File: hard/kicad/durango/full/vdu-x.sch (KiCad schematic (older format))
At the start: 48 parts, among them J105 SCART, J4 LED, Q306 BC548, Q4 BC548, Q5 BC548, U124 74HC574, U125 74HC157, U126 HC86, U127 74HC245, U15 74HCT4040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

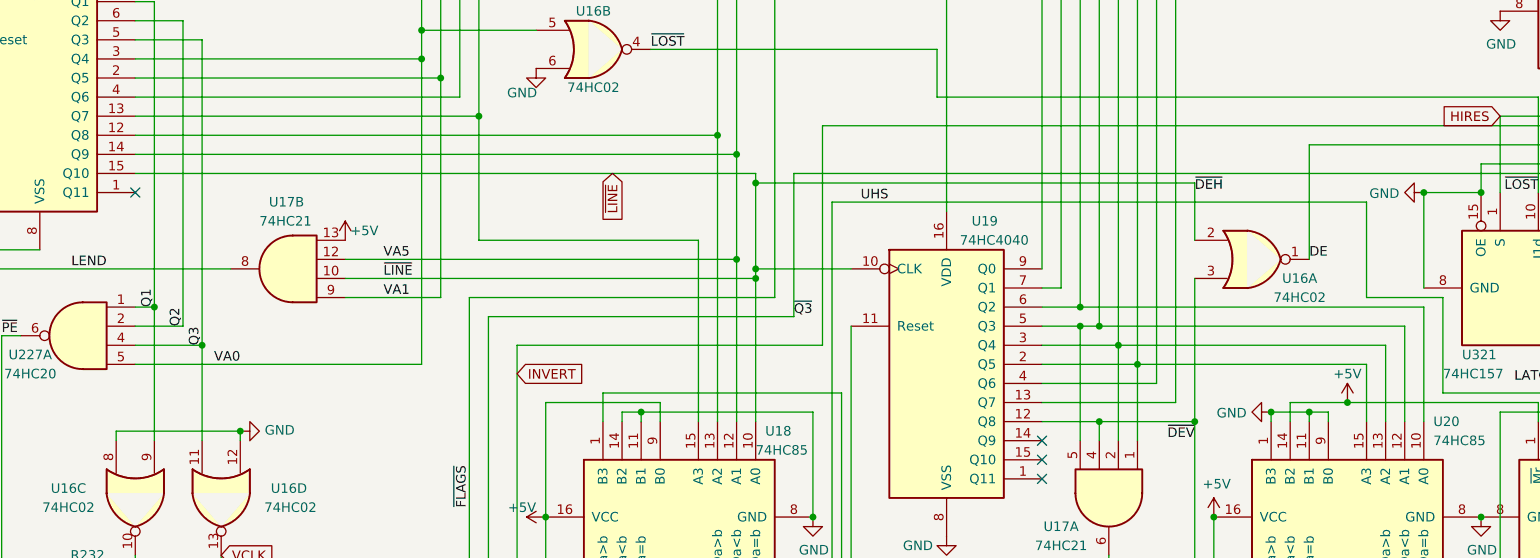
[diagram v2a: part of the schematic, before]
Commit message: PINOUT: rewire HC85s
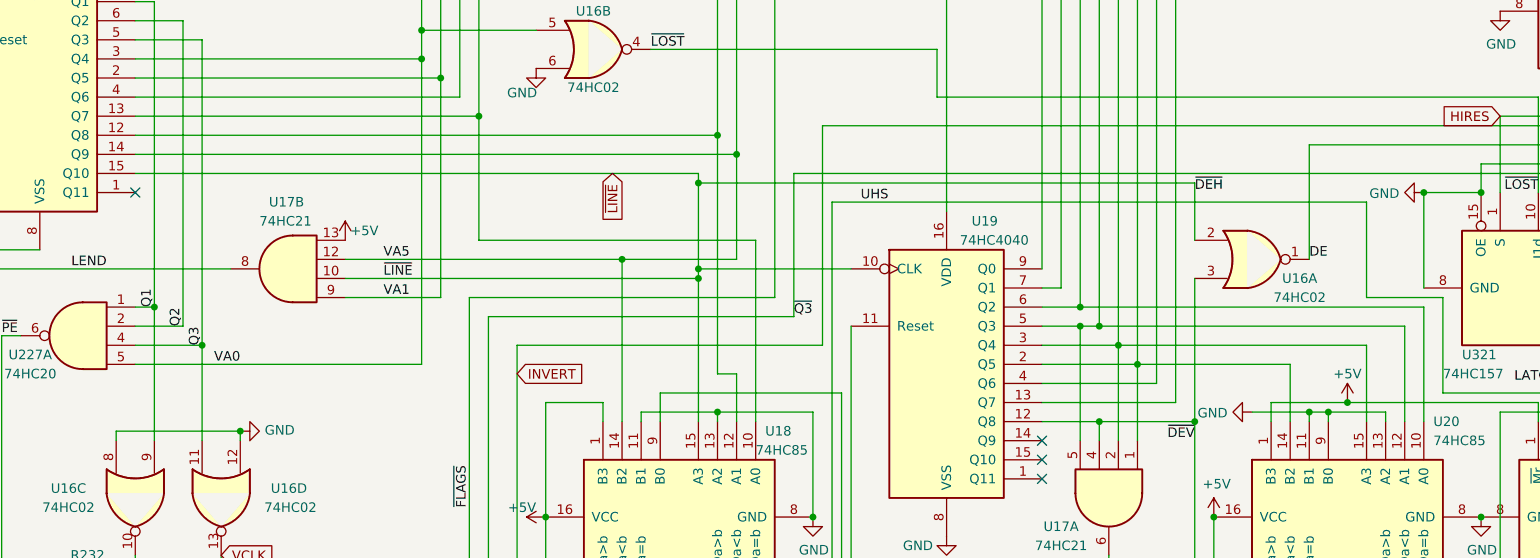
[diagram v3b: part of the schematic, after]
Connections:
- net +5V: now also U18.1 (B3), U20.1 (B3); no longer U18.9 (B0), U20.14 (B2)
- net GND: now also U18.13 (A2), U20.13 (A2); no longer U18.14 (B2), U20.1 (B3)
- net VA10: now also U20.15 (A3); no longer U20.13 (A2)
- net VA11: now also U20.14 (B2); no longer U20.15 (A3)
- net VA3: now also U18.10 (A0); no longer U18.15 (A3)
- net VA4: now also U18.12 (A1); no longer U18.13 (A2)
- net VA5: now also U18.14 (B2); no longer U18.12 (A1)
- net ~LINE: now also U18.15 (A3); no longer U18.10 (A0)
- net ~VS: now also U18.9 (B0); no longer U18.1 (B3)
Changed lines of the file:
@@
 Connection ~ 4650 3900
 Wire Wire Line
-	5250 3400 5250 3300
-Wire Wire Line
 	4650 3300 4650 3900
-Wire Wire Line
-	5150 3400 5150 3350
-Wire Wire Line
-	5150 3350 6050 3350
 Wire Wire Line
 	6050 3350 6050 3900
@@
 	5050 4400 5150 4400
 Wire Wire Line
-	5150 3350 5050 3350
-Wire Wire Line
-	5050 3350 5050 3400
-Connection ~ 5150 3350
-Wire Wire Line
 	8050 3400 8050 4450
 Wire Wire Line
@@
 Connection ~ 8050 3400
 Wire Wire Line
-	7750 3100 8950 3100
-Wire Wire Line
-	8950 3100 8950 3400
-Wire Wire Line
-	7650 3000 9050 3000
-Wire Wire Line
-	9050 3000 9050 3400
+	7750 3100 8550 3100
+Wire Wire Line
+	7650 3000 8950 3000
 Wire Wire Line
 	7550 2900 9150 2900
-Wire Wire Line
-	9150 2900 9150 3400
 Connection ~ 7550 2900
 Wire Wire Line
 	7450 2800 9250 2800
-Wire Wire Line
-	9250 2800 9250 3400
 Connection ~ 7450 2800
-Wire Wire Line
-	8450 3400 8450 3350
-Wire Wire Line
-	8450 3350 8650 3350
-Wire Wire Line
-	8650 3350 8650 3400
-Wire Wire Line
-	8550 3400 8550 3300
 $Comp
 L power:+5V #PWR0122
@@
 L power:GND #PWR0123
 U 1 1 608EF4C1
-P 8450 3350
-F 0 "#PWR0123" H 8450 3100 50  0001 C CNN
-F 1 "GND" V 8455 3222 50  0000 R CNN
-F 2 "" H 8450 3350 50  0001 C CNN
-F 3 "" H 8450 3350 50  0001 C CNN
-	1    8450 3350
+P 8350 3350
+F 0 "#PWR0123" H 8350 3100 50  0001 C CNN
+F 1 "GND" V 8355 3222 50  0000 R CNN
+F 2 "" H 8350 3350 50  0001 C CNN
+F 3 "" H 8350 3350 50  0001 C CNN
+	1    8350 3350
 	0    1    1    0
 $EndComp
-Connection ~ 8450 3350
 Wire Wire Line
 	6250 2900 6250 4250
@@
 	8050 2450 8050 2150
 Wire Wire Line
-	8050 2150 5750 2150
-Connection ~ 5750 2150
-Wire Wire Line
 	10950 3250 10950 5650
 Text GLabel 8800 550  0    50   Input ~ 0
@@
 $EndComp
 Wire Wire Line
-	4300 2450 5450 2450
-Wire Wire Line
-	5450 2450 5450 3400
+	4300 2450 5750 2450
 $Comp
 L 74xx:74LS20 U227
@@
 VA1
 Wire Wire Line
-	3600 2550 5650 2550
-Connection ~ 5650 2550
-Wire Wire Line
-	3600 2650 5750 2650
-Wire Wire Line
-	5750 2150 5750 2600
-Connection ~ 5750 2650
+	3600 2550 5050 2550
+Wire Wire Line
+	3600 2650 5450 2650
 Text Label 3800 2650 0    50   ~ 0
 ~LINE
@@
 Wire Wire Line
 	2500 1900 5550 1900
-Connection ~ 5550 1900
-Wire Wire Line
-	5550 1900 5550 3400
 Wire Wire Line
 	2500 2000 5650 2000
@@
 	5650 2000 5650 2550
 Wire Wire Line
-	2500 2100 5750 2100
-Wire Wire Line
-	5750 2100 5750 2150
+	2500 2100 5450 2100
 NoConn ~ 2500 2200
 Wire Wire Line
@@
 Wire Wire Line
 	4000 1350 4000 1500
-Wire Wire Line
-	5650 2550 5650 3400
 Wire Wire Line
 	6700 1700 6700 1450
@@
 Wire Wire Line
 	1200 2500 2000 2500
-Wire Wire Line
-	5750 2650 5750 3400
 Wire Wire Line
 	4350 2850 5950 2850
@@
 Wire Wire Line
 	7600 4400 6200 4400
-Wire Wire Line
-	6200 4400 6200 3250
 Connection ~ 10050 4400
 Text Label 7050 4400 0    50   ~ 0
 ~VS
 Wire Wire Line
-	4650 3300 5250 3300
-Wire Wire Line
-	4950 3400 4950 3250
-Wire Wire Line
-	4950 3250 6200 3250
+	4650 3300 4950 3300
 Wire Wire Line
 	6150 2250 6150 4400
-Wire Wire Line
-	6250 2600 5750 2600
-Connection ~ 5750 2600
-Wire Wire Line
-	5750 2600 5750 2650
 Text Label 6300 2250 0    50   ~ 0
 UHS
 Wire Wire Line
-	8650 3350 8750 3350
-Wire Wire Line
-	8750 3350 8750 3400
-Connection ~ 8650 3350
-Wire Wire Line
-	8550 3300 8850 3300
+	8450 3300 8850 3300
 Connection ~ 8850 3300
 Wire Wire Line
@@
 Wire Wire Line
 	750  5900 800  5900
+Wire Wire Line
+	5150 3350 5550 3350
+Wire Wire Line
+	4950 3400 4950 3300
+Wire Wire Line
+	5150 3350 5150 3400
+Wire Wire Line
+	5550 3350 5550 3400
+Connection ~ 5550 3350
+Wire Wire Line
+	5550 3350 6050 3350
+Wire Wire Line
+	6200 4400 6200 3250
+Wire Wire Line
+	5250 3250 6200 3250
+Wire Wire Line
+	5250 3400 5250 3250
+Wire Wire Line
+	5050 3400 5050 2550
+Connection ~ 5050 2550
+Wire Wire Line
+	5050 2550 5650 2550
+Connection ~ 5450 2600
+Wire Wire Line
+	6250 2600 5450 2600
+Wire Wire Line
+	5450 2100 5450 2150
+Wire Wire Line
+	5450 2150 5450 2600
+Connection ~ 5450 2150
+Wire Wire Line
+	8050 2150 5450 2150
+Wire Wire Line
+	5450 2600 5450 2650
+Connection ~ 5450 2650
+Wire Wire Line
+	5450 2650 5450 3400
+Wire Wire Line
+	5550 1900 5550 3150
+Wire Wire Line
+	5550 3150 5650 3150
+Wire Wire Line
+	5650 3150 5650 3400
+Connection ~ 5550 1900
+Wire Wire Line
+	5750 2450 5750 3400
+Wire Wire Line
+	8350 3350 8650 3350
+Wire Wire Line
+	8450 3300 8450 3400
+Wire Wire Line
+	8650 3350 8650 3400
+Connection ~ 8650 3350
+Wire Wire Line
+	8650 3350 8750 3350
+Wire Wire Line
+	8750 3350 8750 3400
+Wire Wire Line
+	8750 3350 9050 3350
+Wire Wire Line
+	9050 3350 9050 3400
+Connection ~ 8750 3350
+Wire Wire Line
+	8550 3100 8550 3400
+Wire Wire Line
+	8950 3000 8950 3400
+Wire Wire Line
+	9250 2800 9250 3400
+Wire Wire Line
+	9150 3400 9150 2900
 Wire Bus Line
 	8800 550  10750 550

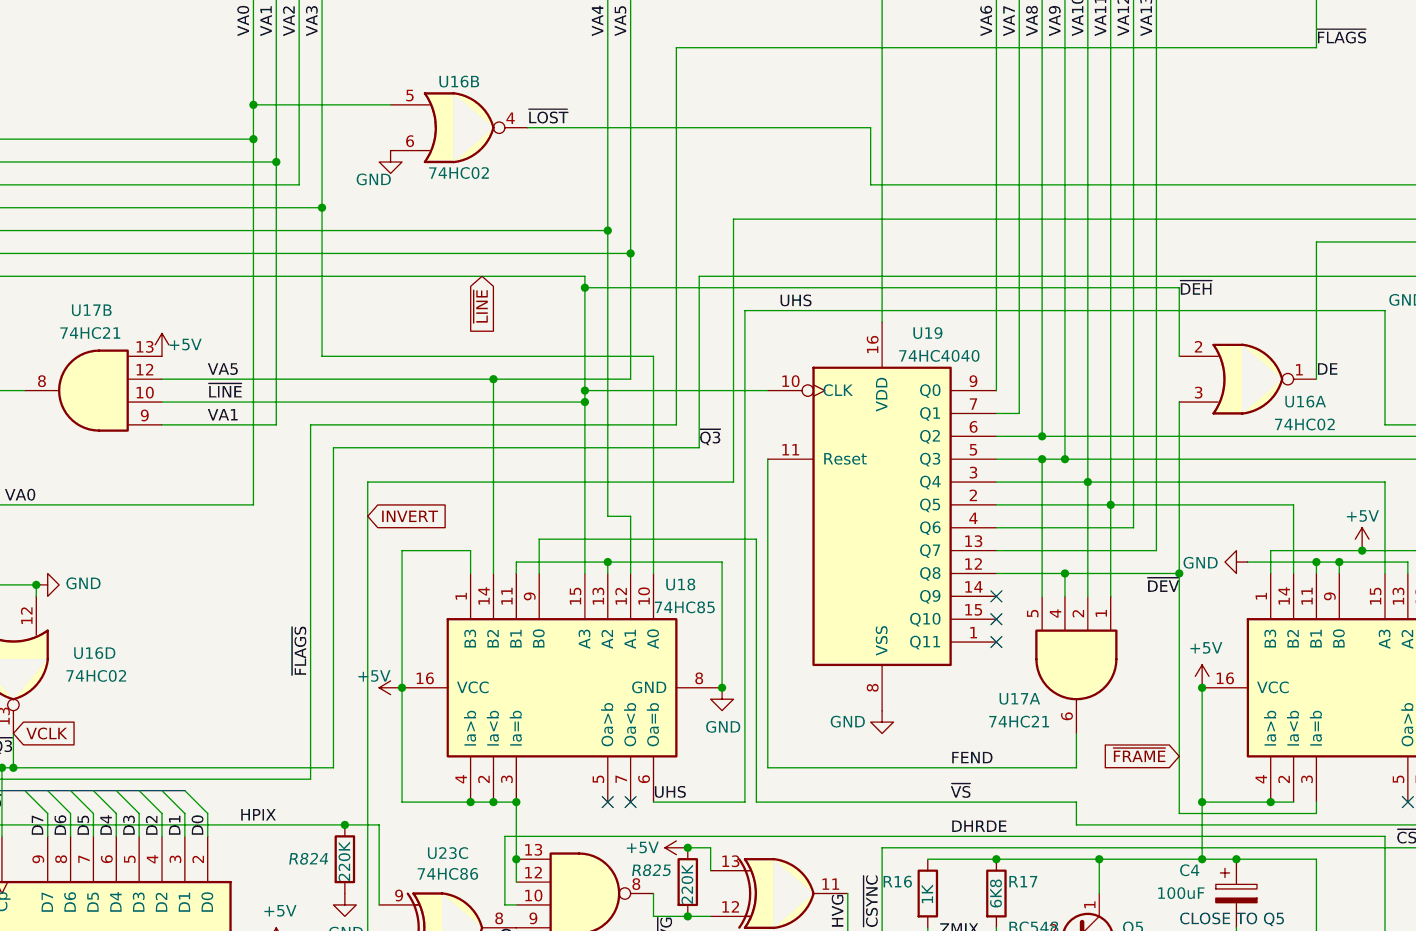
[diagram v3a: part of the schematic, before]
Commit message: PINOUT: rewire HC21
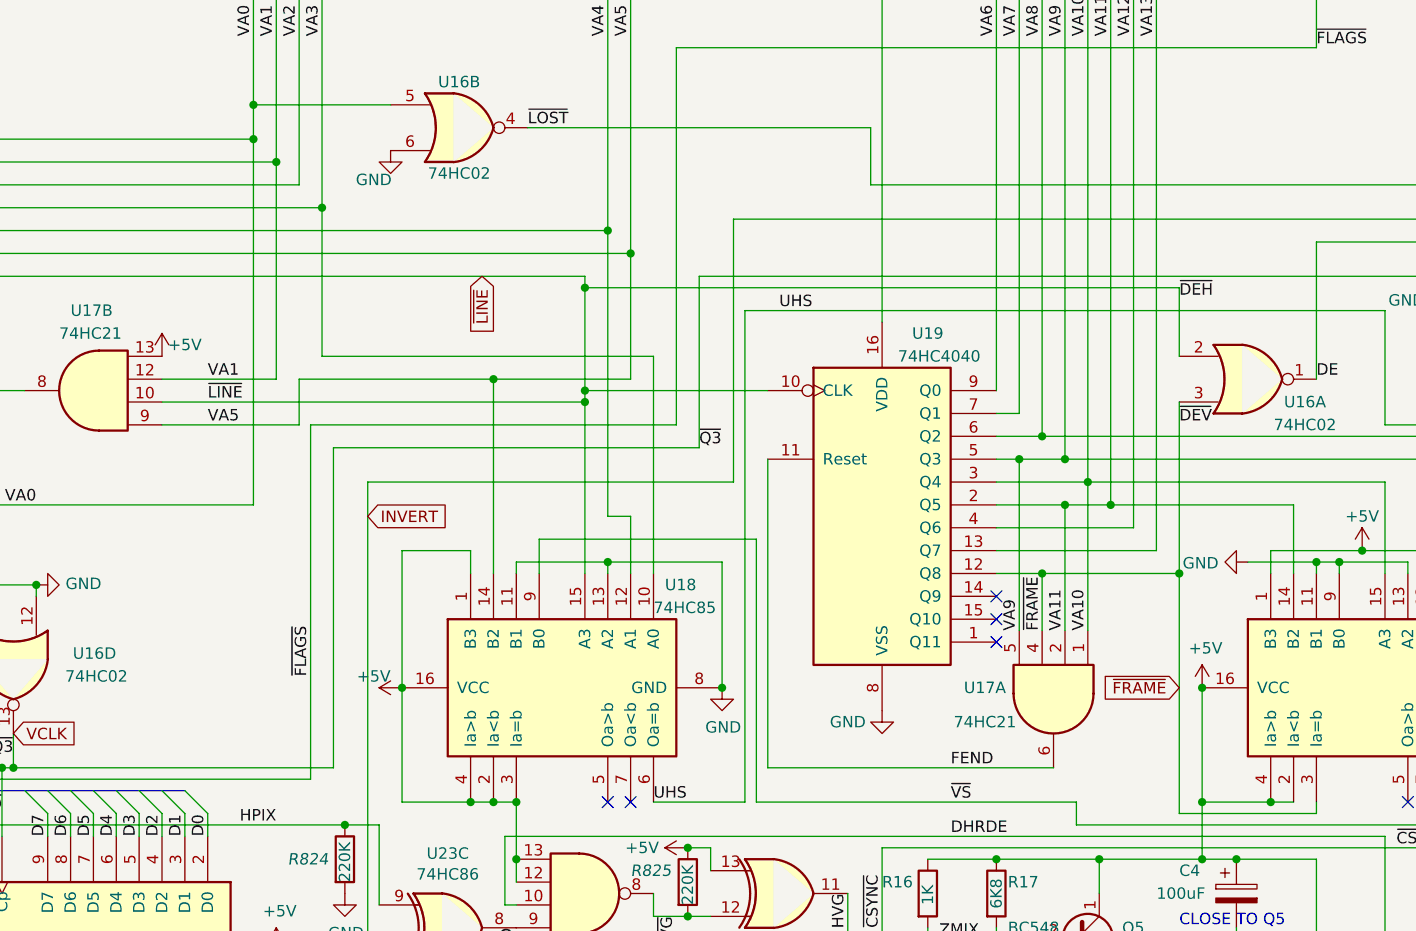
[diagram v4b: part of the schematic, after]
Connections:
- net VA1: now also U17.12; no longer U17.9
- net VA10: now also U17.1; no longer U17.2
- net VA11: now also U17.2; no longer U17.1
- net VA5: now also U17.9; no longer U17.12
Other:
- moved on the sheet: U17A
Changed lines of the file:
@@
 	7450 2800 7450 650
 Wire Wire Line
-	7250 2900 7450 2900
+	7250 2900 7350 2900
 Wire Wire Line
 	7550 2900 7550 650
@@
 Wire Wire Line
 	7650 3000 7650 650
-Wire Wire Line
-	7250 3100 7750 3100
 Wire Wire Line
 	7750 3100 7750 650
@@
 $EndComp
 Wire Wire Line
-	7250 3400 7550 3400
-Wire Wire Line
-	7750 3500 7750 3100
+	7250 3400 7450 3400
 Connection ~ 7750 3100
-Wire Wire Line
-	7650 3000 7650 3500
 Connection ~ 7650 3000
 Wire Wire Line
-	7450 2900 7450 3500
-Connection ~ 7450 2900
-Wire Wire Line
-	7450 2900 7550 2900
-Wire Wire Line
-	7250 3200 7850 3200
-Wire Wire Line
-	7550 3500 7550 3400
-Connection ~ 7550 3400
-Wire Wire Line
-	7550 3400 8050 3400
+	7350 2900 7350 3650
+Connection ~ 7350 2900
+Wire Wire Line
+	7350 2900 7550 2900
+Wire Wire Line
+	7450 3650 7450 3400
+Connection ~ 7450 3400
+Wire Wire Line
+	7450 3400 8050 3400
 Text Label 7950 1050 1    50   ~ 0
 VA13
@@
 Text Label 8050 2200 0    50   ~ 0
 ~DEH
-Text Label 8050 3500 2    50   ~ 0
+Text Label 8050 2750 0    50   ~ 0
 ~DEV
 Wire Wire Line
@@
 	6250 2900 6250 4250
 Wire Wire Line
-	6250 4250 7600 4250
+	6250 4250 7500 4250
 Wire Wire Line
 	5750 4400 6150 4400
@@
 Wire Wire Line
 	6600 4800 6600 5150
-Wire Wire Line
-	7600 4250 7600 4100
 $Comp
 L 74xx:74HCT02 U16
@@
 Text Label 3050 3100 2    50   ~ 0
 VA0
-Wire Wire Line
-	3600 2750 4100 2750
-Text Label 3800 2750 0    50   ~ 0
+Text Label 3800 2550 0    50   ~ 0
 VA1
-Wire Wire Line
-	3600 2550 5050 2550
 Wire Wire Line
 	3600 2650 5450 2650
 Text Label 3800 2650 0    50   ~ 0
 ~LINE
-Text Label 3800 2550 0    50   ~ 0
+Text Label 3800 2750 0    50   ~ 0
 VA5
 Text Label 2850 3000 1    50   ~ 0
@@
 Text GLabel 4500 3150 2    50   Input ~ 0
 INVERT
-Text GLabel 8050 4200 0    50   Input ~ 0
+Text GLabel 8050 3900 0    50   Input ~ 0
 ~FRAME
 Text GLabel 5000 2100 3    50   Input ~ 0
@@
 L 74xx:74LS21 U17
 U 1 1 615D7357
-P 7600 3800
-F 0 "U17" V 7750 3550 50  0000 C CNN
-F 1 "74HC21" V 7850 3550 50  0000 C CNN
-F 2 "Package_DIP:DIP-14_W7.62mm_Socket" H 7600 3800 50  0001 C CNN
-F 3 "http://www.ti.com/lit/gpn/sn74LS21" H 7600 3800 50  0001 C CNN
-	1    7600 3800
+P 7500 3950
+F 0 "U17" V 7450 3650 50  0000 C CNN
+F 1 "74HC21" V 7600 3650 50  0000 C CNN
+F 2 "Package_DIP:DIP-14_W7.62mm_Socket" H 7500 3950 50  0001 C CNN
+F 3 "http://www.ti.com/lit/gpn/sn74LS21" H 7500 3950 50  0001 C CNN
+	1    7500 3950
 	0    1    1    0
 $EndComp
@@
 Connection ~ 4100 1600
 Wire Wire Line
-	4100 1600 4100 2750
+	4100 1600 4100 2550
 Wire Wire Line
 	4200 1700 2500 1700
@@
 Wire Wire Line
 	5050 3400 5050 2550
-Connection ~ 5050 2550
 Wire Wire Line
 	5050 2550 5650 2550
@@
 Wire Wire Line
 	9150 3400 9150 2900
+Wire Wire Line
+	7650 3000 7650 3650
+Wire Wire Line
+	7250 3200 7850 3200
+Wire Wire Line
+	7550 3100 7550 3650
+Wire Wire Line
+	7250 3100 7550 3100
+Connection ~ 7550 3100
+Wire Wire Line
+	7550 3100 7750 3100
+Wire Wire Line
+	4100 2550 3600 2550
+Wire Wire Line
+	5050 2550 4200 2550
+Wire Wire Line
+	4200 2550 4200 2750
+Wire Wire Line
+	3600 2750 4200 2750
+Connection ~ 5050 2550
 Wire Bus Line
 	8800 550  10750 550
@@
 Wire Bus Line
 	800  4350 3700 4350
+Text Label 7650 3650 1    50   ~ 0
+VA10
+Text Label 7550 3650 1    50   ~ 0
+VA11
+Text Label 7450 3650 1    50   ~ 0
+~FRAME
+Text Label 7350 3650 1    50   ~ 0
+VA9
 $EndSCHEMATC
